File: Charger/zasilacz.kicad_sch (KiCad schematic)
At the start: 0 parts

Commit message: dodanie sekcji zasilacza
i dodanie footprintów prawie wszedzie
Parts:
- added C24, C25: 470u, Library:CP_Elec_12.5x13.5, symbol Device:C_Polarized
- added C26, C30: 22u, Capacitor_SMD:CP_Elec_4x5.4, symbol Device:C_Polarized
- added C27, C28, C29, C31: 100n, Capacitor_SMD:C_0805_2012Metric_Pad1.18x1.45mm_HandSolder, symbol Device:C
- added D6: SS26, Diode_SMD:D_SMA, symbol Diode:SS26
- added L3: 330u, Inductor_SMD:L_Bourns_SRR1208_12.7x12.7mm, symbol Device:L
- added U20: LM2575-12BU, Package_TO_SOT_SMD:TO-263-5_TabPin3, symbol Regulator_Switching:LM2575-12BU
- added U21: L7805, Package_TO_SOT_SMD:TO-263-2, symbol Regulator_Linear:L7805
- added U22: LDI1117-3.3, Package_TO_SOT_SMD:SOT-223-3_TabPin2, symbol Regulator_Linear:AZ1117-3.3
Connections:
- new net: D6.1 (K), L3.1, U20.2 (OUT)
- new net +12V: C24.1, C28.1, C31.1, L3.2, U20.4 (FB), U21.1 (IN), U22.3 (VI)
- new net +3.3V: C29.1, C30.1, U22.2 (VO)
- new net +5V: C26.1, C27.1, U21.3 (OUT)
- new net GND: C24.2, C25.2, C26.2, C27.2, C28.2, C29.2, C30.2, C31.2, D6.2 (A), U20.3 (GND), U20.5 (~{ON}/OFF), U21.2 (GND), U22.1 (GND)
- new net Z+: C25.1, U20.1 (VIN)

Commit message: drobne zmiany
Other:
- moved on the sheet: C31
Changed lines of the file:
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@@
+	)
+	(junction
+		(at 125.73 128.27)
+		(diameter 0)
+		(color 0 0 0 0)
 	)
 	(junction
@@
 	)
 	(junction
-		(at 127 128.27)
-		(diameter 0)
-		(color 0 0 0 0)
-	)
-	(junction
 		(at 148.59 128.27)
 		(diameter 0)
@@
 	(wire
 		(pts
-			(xy 124.46 128.27) (xy 127 128.27)
+			(xy 124.46 128.27) (xy 125.73 128.27)
 		)
 		(stroke
@@
 	(wire
 		(pts
+			(xy 125.73 128.27) (xy 130.81 128.27)
+		)
+		(stroke
+			(width 0)
+			(type default)
+		)
+	)
+	(wire
+		(pts
 			(xy 148.59 128.27) (xy 158.75 128.27)
 		)
@@
 	(wire
 		(pts
-			(xy 127 128.27) (xy 130.81 128.27)
-		)
-		(stroke
-			(width 0)
-			(type default)
-		)
-	)
-	(wire
-		(pts
 			(xy 116.84 62.23) (xy 116.84 64.77)
 		)
@@
 	(wire
 		(pts
-			(xy 127 135.89) (xy 138.43 135.89)
+			(xy 125.73 135.89) (xy 138.43 135.89)
 		)
 		(stroke
@@
 		(on_board yes)
 		(dnp no)
-		(fields_autoplaced yes)
 		(property "Reference" "C28"
-			(at 128.27 99.0599 0)
+			(at 127 99.06 0)
 			(effects
 				(font
@@
 		)
 		(property "Value" "100n"
-			(at 128.27 101.5999 0)
+			(at 127 101.6 0)
 			(effects
 				(font
@@
 	(symbol
 		(lib_id "Device:C")
-		(at 127 132.08 0)
+		(at 125.73 132.08 0)
 		(unit 1)
 		(exclude_from_sim no)
@@
 		(on_board yes)
 		(dnp no)
-		(fields_autoplaced yes)
 		(property "Reference" "C31"
-			(at 130.81 130.8099 0)
+			(at 128.27 130.81 0)
 			(effects
 				(font
@@
 		)
 		(property "Value" "100n"
-			(at 130.81 133.3499 0)
+			(at 128.27 133.35 0)
 			(effects
 				(font
@@
 		)
 		(property "Footprint" "Capacitor_SMD:C_0805_2012Metric_Pad1.18x1.45mm_HandSolder"
-			(at 127.9652 135.89 0)
+			(at 126.6952 135.89 0)
 			(effects
 				(font
@@
 		)
 		(property "Datasheet" "~"
-			(at 127 132.08 0)
+			(at 125.73 132.08 0)
 			(effects
 				(font
@@
 		)
 		(property "Description" "Unpolarized capacitor"
-			(at 127 132.08 0)
+			(at 125.73 132.08 0)
 			(effects
 				(font
@@
 		(on_board yes)
 		(dnp no)
-		(fields_autoplaced yes)
 		(property "Reference" "C30"
-			(at 162.56 129.9209 0)
+			(at 161.29 130.81 0)
 			(effects
 				(font
@@
 		)
 		(property "Value" "22u"
-			(at 162.56 132.4609 0)
+			(at 161.29 133.35 0)
 			(effects
 				(font
@@
 		(on_board yes)
 		(dnp no)
-		(fields_autoplaced yes)
 		(property "Reference" "C29"
-			(at 152.4 130.8099 0)
+			(at 150.876 130.81 0)
 			(effects
 				(font
@@
 		)
 		(property "Value" "100n"
-			(at 152.4 133.3499 0)
+			(at 150.876 133.35 0)
 			(effects
 				(font
@@
 		(on_board yes)
 		(dnp no)
-		(fields_autoplaced yes)
 		(property "Reference" "C26"
-			(at 163.83 98.1709 0)
+			(at 162.56 99.06 0)
 			(effects
 				(font
@@
 		)
 		(property "Value" "22u"
-			(at 163.83 100.7109 0)
-			(effects
-				(font
+			(at 162.56 101.6 0)
+			(effects
+				(font

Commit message: pcb up
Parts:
- added C38: 100n, Capacitor_SMD:C_0805_2012Metric_Pad1.18x1.45mm_HandSolder, symbol Device:C
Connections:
- net +12V: now also C38.1
- net GND: now also C38.2

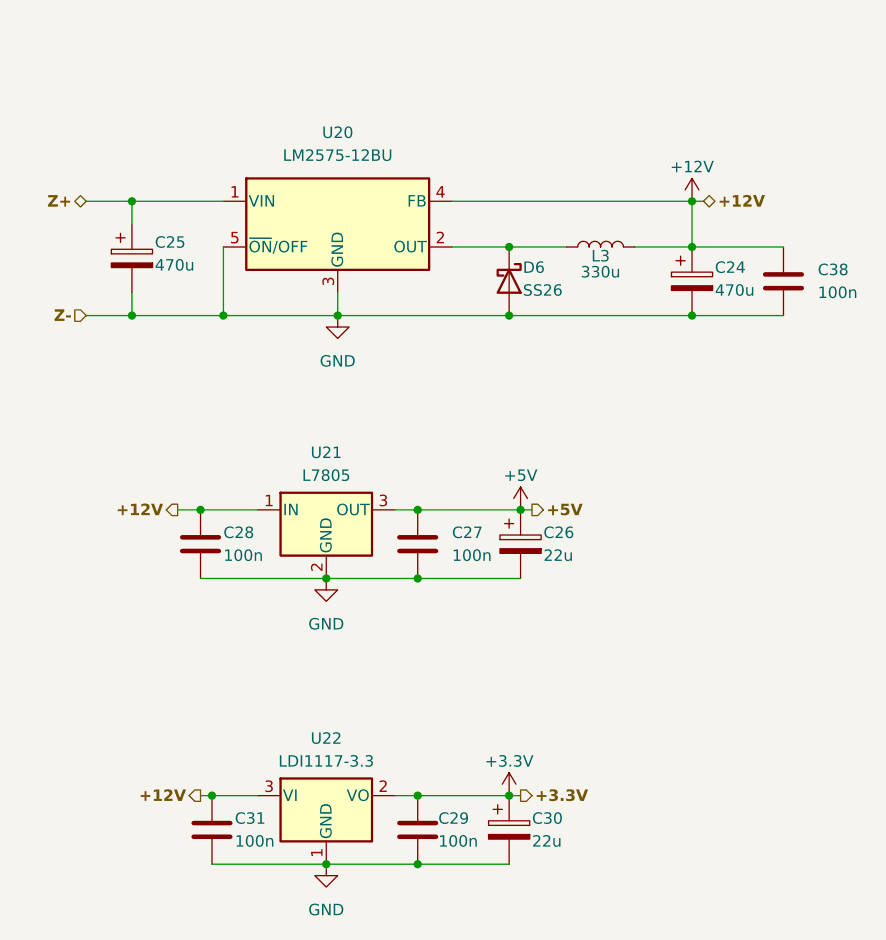
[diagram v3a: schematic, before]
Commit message: aktualizacja schematu
nie zmieniałem nic na pcb
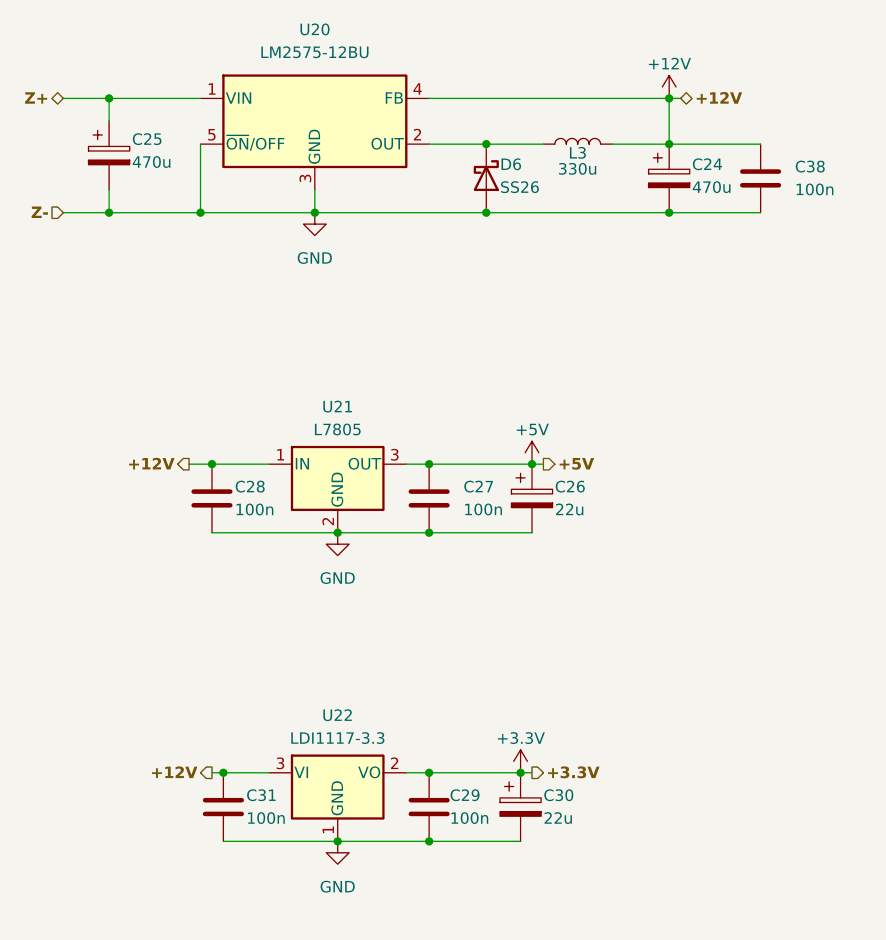
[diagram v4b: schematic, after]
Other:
- moved on the sheet: C24, C25, C26, C27, C28, C29, C30, C31, C38, D6, L3, U20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
